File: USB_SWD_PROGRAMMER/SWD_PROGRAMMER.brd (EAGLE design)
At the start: 99.5 x 49.1 mm, 19 parts, among them J1 USB_B, SW1 CJS, SW2 CJS, U1 KW2_CPU_OFFSET, U2 KL20PAD, X1 CSTCE8M00G55-R0

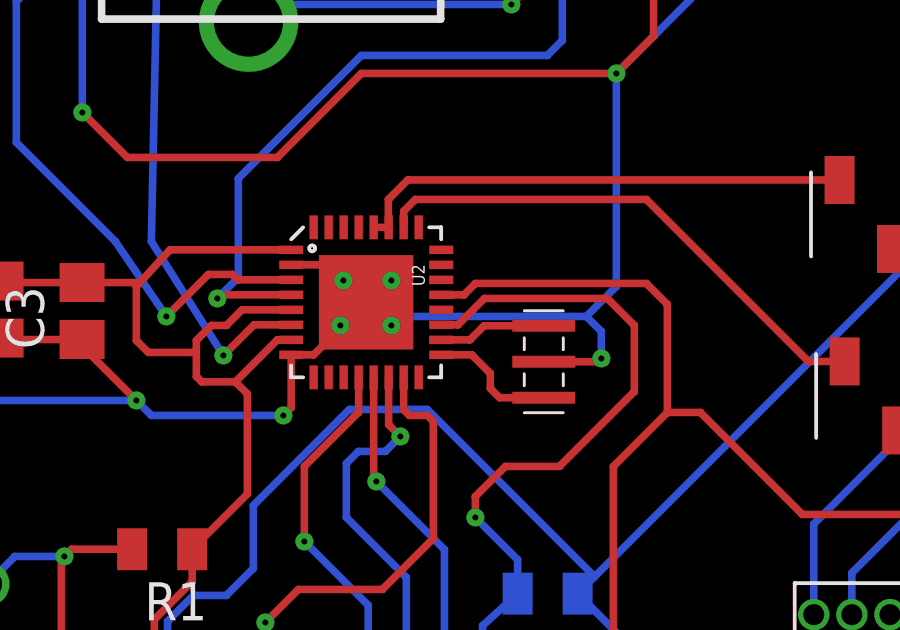
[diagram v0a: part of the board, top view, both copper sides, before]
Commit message: Misc changes (SWD)
Misc changes (SWD)
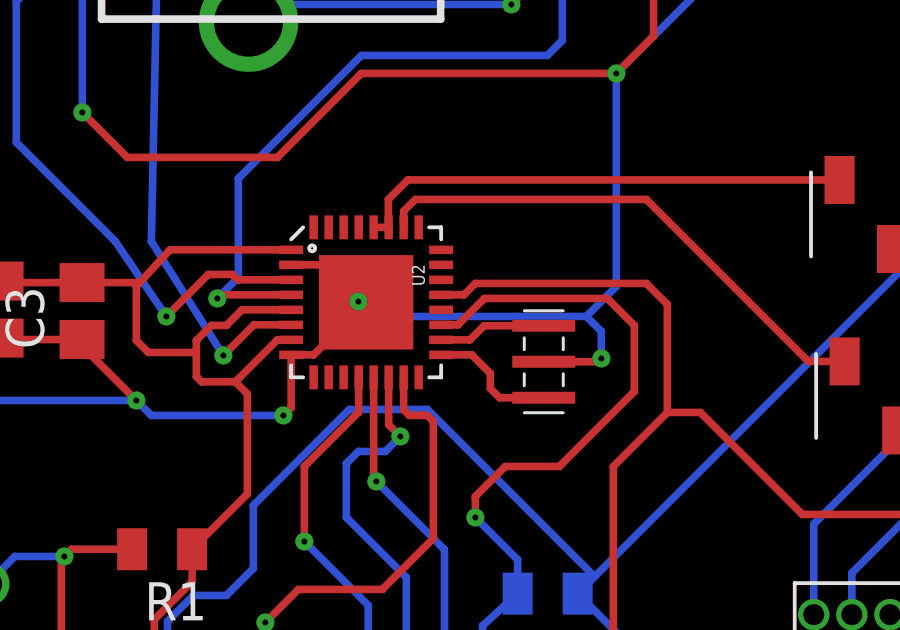
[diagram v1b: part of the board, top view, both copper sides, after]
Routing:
- net GND: track 244.0 -> 244.1 mm, vias 10 -> 7
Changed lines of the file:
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@@
 <?xml version="1.0" encoding="utf-8"?>
 <!DOCTYPE eagle SYSTEM "eagle.dtd">
-<eagle version="7.5.0">
+<eagle version="6.5.0">
 <drawing>
 <settings>
@@
 <pass name="Default">
 <param name="RoutingGrid" value="50mil"/>
-<param name="AutoGrid" value="1"/>
-<param name="Efforts" value="0"/>
-<param name="TopRouterVariant" value="1"/>
 <param name="tpViaShape" value="round"/>
-<param name="PrefDir.1" value="a"/>
+<param name="PrefDir.1" value="|"/>
 <param name="PrefDir.2" value="0"/>
 <param name="PrefDir.3" value="0"/>
@@
 <param name="PrefDir.14" value="0"/>
 <param name="PrefDir.15" value="0"/>
-<param name="PrefDir.16" value="a"/>
+<param name="PrefDir.16" value="-"/>
 <param name="cfVia" value="8"/>
 <param name="cfNonPref" value="5"/>
@@
 <contactref element="U2" pad="EP"/>
 <wire x1="34.26" y1="46.72" x2="35.01" y2="46.72" width="0.254" layer="1"/>
-<wire x1="35.01" y1="46.72" x2="36.76" y2="48.47" width="0.254" layer="1"/>
+<wire x1="35.01" y1="46.72" x2="35.99" y2="47.7" width="0.254" layer="1"/>
+<wire x1="35.99" y1="47.7" x2="36.76" y2="48.47" width="0.254" layer="1"/>
 <wire x1="34.26" y1="49.72" x2="35.51" y2="49.72" width="0.254" layer="1"/>
 <wire x1="35.51" y1="49.72" x2="36.03" y2="49.2" width="0.254" layer="1"/>
-<wire x1="36.03" y1="49.2" x2="36.76" y2="48.47" width="0.254" layer="1"/>
 <wire x1="46.26" y1="65.81" x2="46.26" y2="62.89" width="0.254" layer="1"/>
 <wire x1="46.26" y1="62.89" x2="46.26" y2="59.98" width="0.254" layer="1"/>
 <wire x1="46.26" y1="59.98" x2="46.34" y2="59.9" width="0.254" layer="1"/>
-<via x="37.6" y="47.7" extent="1-16" drill="0.2"/>
-<via x="35.9" y="47.7" extent="1-16" drill="0.2"/>
-<via x="36" y="49.2" extent="1-16" drill="0.2"/>
-<via x="37.6" y="49.2" extent="1-16" drill="0.2"/>
 <wire x1="36" y1="49.2" x2="36.03" y2="49.2" width="0.254" layer="1"/>
-<wire x1="37.6" y1="49.2" x2="37.49" y2="49.2" width="0.254" layer="1"/>
-<wire x1="37.49" y1="49.2" x2="36.76" y2="48.47" width="0.254" layer="1"/>
 <wire x1="37.6" y1="47.7" x2="37.53" y2="47.7" width="0.254" layer="1"/>
-<wire x1="37.53" y1="47.7" x2="36.76" y2="48.47" width="0.254" layer="1"/>
 <wire x1="35.9" y1="47.7" x2="35.99" y2="47.7" width="0.254" layer="1"/>
-<wire x1="35.99" y1="47.7" x2="36.76" y2="48.47" width="0.254" layer="1"/>
 <via x="44.6" y="46.6" extent="1-16" drill="0.2"/>
-<wire x1="44.1" y1="48" x2="37.9" y2="48" width="0.254" layer="16"/>
-<wire x1="37.9" y1="48" x2="37.6" y2="47.7" width="0.254" layer="16"/>
 <wire x1="36.83" y1="34.89" x2="38.1" y2="34.89" width="0.254" layer="16"/>
 <wire x1="38.1" y1="34.89" x2="38.1" y2="31.9" width="0.254" layer="16"/>
@@
 <wire x1="29.1" y1="45.2" x2="27.29" y2="47.01" width="0.254" layer="1"/>
 <wire x1="27.29" y1="47.01" x2="27.29" y2="47.23" width="0.254" layer="1"/>
+<wire x1="44.1" y1="48" x2="37.23" y2="48" width="0.254" layer="16"/>
+<wire x1="37.23" y1="48" x2="36.76" y2="48.47" width="0.254" layer="16"/>
+<via x="36.5" y="48.5" extent="1-16" drill="0.2"/>
+<wire x1="36.5" y1="48.5" x2="36.73" y2="48.5" width="0.254" layer="16"/>
+<wire x1="36.73" y1="48.5" x2="36.76" y2="48.47" width="0.254" layer="16"/>
+<wire x1="36.03" y1="49.2" x2="36.03" y2="48.97" width="0.254" layer="1"/>
+<wire x1="36.03" y1="48.97" x2="36.5" y2="48.5" width="0.254" layer="1"/>
+<wire x1="35.99" y1="47.7" x2="35.99" y2="47.99" width="0.254" layer="1"/>
+<wire x1="35.99" y1="47.99" x2="36.5" y2="48.5" width="0.254" layer="1"/>
+<wire x1="37.53" y1="47.7" x2="37.3" y2="47.7" width="0.254" layer="1"/>
+<wire x1="37.3" y1="47.7" x2="36.5" y2="48.5" width="0.254" layer="1"/>
 </signal>
 <signal name="N$35">

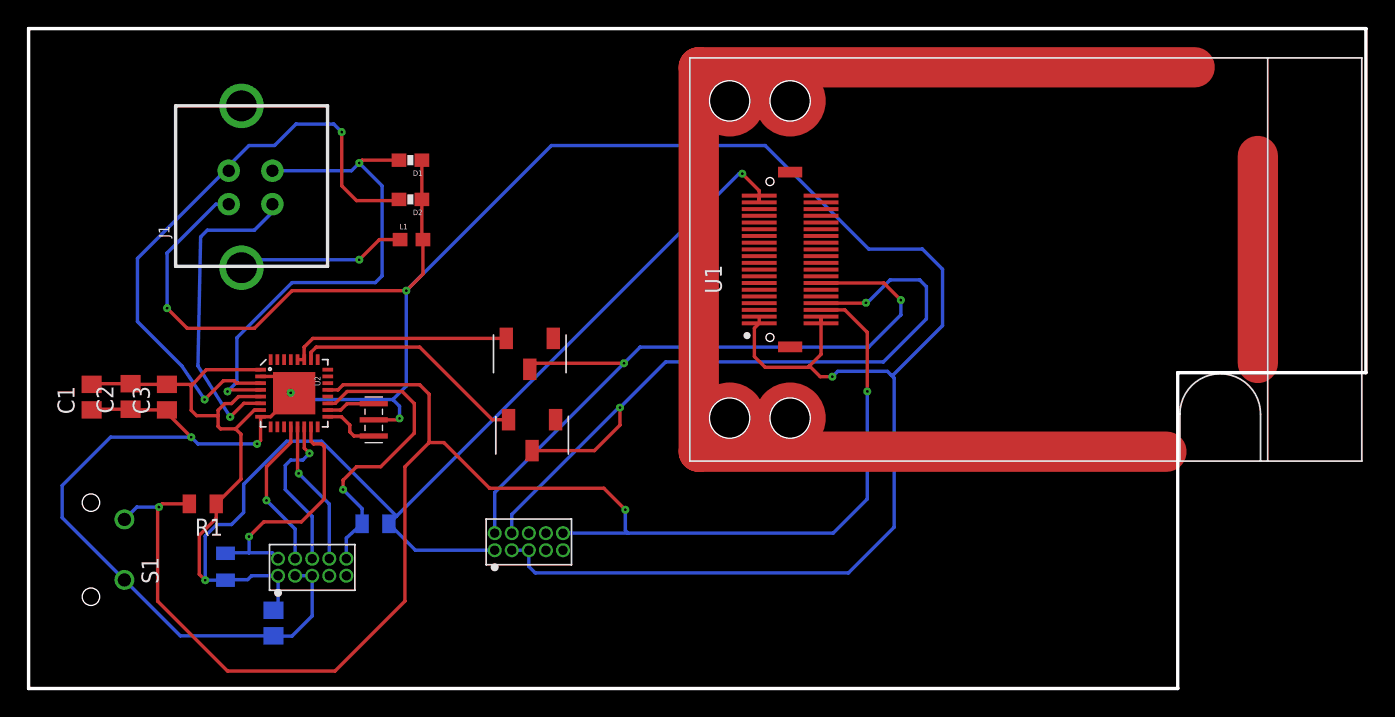
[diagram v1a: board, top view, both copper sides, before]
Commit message: Applied new design rules
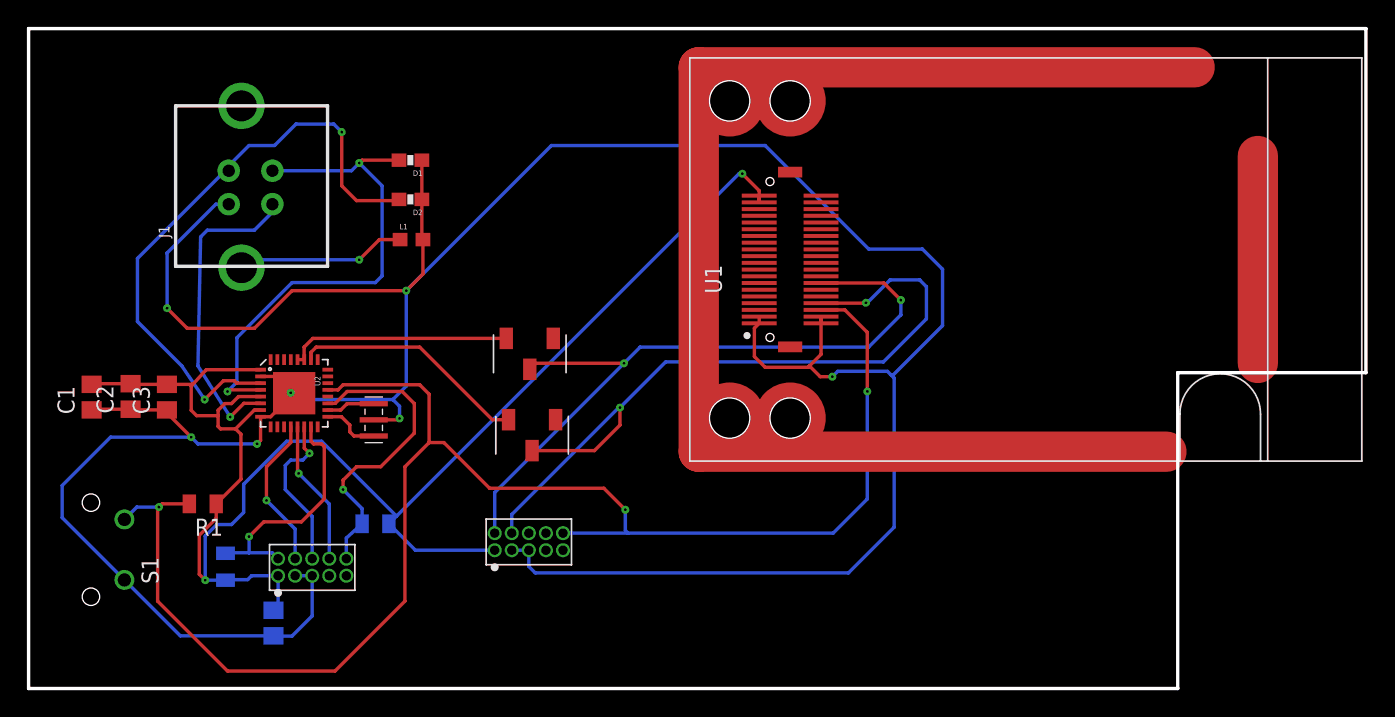
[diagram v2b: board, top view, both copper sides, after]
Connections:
- net N$52 renamed TMS
- net N$55 renamed CLK
- net N$56 renamed TDO
- net N$57 renamed TDI
- net N$58 renamed JRST
- new net N$3: U2.11
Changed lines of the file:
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@@
 </class>
 </classes>
-<designrules name="default *">
-<description language="de">&lt;b&gt;EAGLE Design Rules&lt;/b&gt;
-&lt;p&gt;
-Die Standard-Design-Rules sind so gewählt, dass sie für
-die meisten Anwendungen passen. Sollte ihre Platine
-besondere Anforderungen haben, treffen Sie die erforderlichen
-Einstellungen hier und speichern die Design Rules unter
-einem neuen Namen ab.</description>
+<designrules name="Codeshelf_Standard">
 <description language="en">&lt;b&gt;EAGLE Design Rules&lt;/b&gt;
 &lt;p&gt;
@@
 design rules under a new name.</description>
 <param name="layerSetup" value="(1*16)"/>
-<param name="mtCopper" value="0.035mm 0.035mm 0.035mm 0.035mm 0.035mm 0.035mm 0.035mm 0.035mm 0.035mm 0.035mm 0.035mm 0.035mm 0.035mm 0.035mm 0.035mm 0.035mm"/>
-<param name="mtIsolate" value="1.5mm 0.15mm 0.2mm 0.15mm 0.2mm 0.15mm 0.2mm 0.15mm 0.2mm 0.15mm 0.2mm 0.15mm 0.2mm 0.15mm 0.2mm"/>
-<param name="mdWireWire" value="8mil"/>
-<param name="mdWirePad" value="8mil"/>
-<param name="mdWireVia" value="8mil"/>
-<param name="mdPadPad" value="8mil"/>
-<param name="mdPadVia" value="8mil"/>
-<param name="mdViaVia" value="8mil"/>
-<param name="mdSmdPad" value="8mil"/>
-<param name="mdSmdVia" value="8mil"/>
-<param name="mdSmdSmd" value="8mil"/>
+<param name="mtCopper" value="0.035559375mm 0.035559375mm 0.035559375mm 0.035559375mm 0.0356mm 0.0356mm 0.0356mm 0.0356mm 0.0356mm 0.0356mm 0.0356mm 0.0356mm 0.0356mm 0.0356mm 0.035559375mm 0.035559375mm"/>
+<param name="mtIsolate" value="1.47mm 38mil 10mil 0.1499mm 0.2007mm 0.1499mm 0.2007mm 0.1499mm 0.2007mm 0.1499mm 0.2007mm 0.1499mm 0.2007mm 0.1499mm 10mil"/>
+<param name="mdWireWire" value="0.2mm"/>
+<param name="mdWirePad" value="0.2mm"/>
+<param name="mdWireVia" value="0.2mm"/>
+<param name="mdPadPad" value="0.2mm"/>
+<param name="mdPadVia" value="0.2mm"/>
+<param name="mdViaVia" value="0.2mm"/>
+<param name="mdSmdPad" value="0mil"/>
+<param name="mdSmdVia" value="0mil"/>
+<param name="mdSmdSmd" value="0mil"/>
 <param name="mdViaViaSameLayer" value="8mil"/>
 <param name="mnLayersViaInSmd" value="2"/>
-<param name="mdCopperDimension" value="40mil"/>
-<param name="mdDrill" value="8mil"/>
+<param name="mdCopperDimension" value="0.4mm"/>
+<param name="mdDrill" value="0.5mm"/>
 <param name="mdSmdStop" value="0mil"/>
-<param name="msWidth" value="10mil"/>
-<param name="msDrill" value="24mil"/>
-<param name="msMicroVia" value="9.99mm"/>
+<param name="msWidth" value="0.2mm"/>
+<param name="msDrill" value="0.25mm"/>
+<param name="msMicroVia" value="9.9898mm"/>
 <param name="msBlindViaRatio" value="0.5"/>
 <param name="rvPadTop" value="0.25"/>
@@
 <param name="rvMicroViaOuter" value="0.25"/>
 <param name="rvMicroViaInner" value="0.25"/>
-<param name="rlMinPadTop" value="1mil"/>
-<param name="rlMaxPadTop" value="20mil"/>
-<param name="rlMinPadInner" value="1mil"/>
-<param name="rlMaxPadInner" value="20mil"/>
-<param name="rlMinPadBottom" value="1mil"/>
-<param name="rlMaxPadBottom" value="20mil"/>
-<param name="rlMinViaOuter" value="8mil"/>
-<param name="rlMaxViaOuter" value="20mil"/>
-<param name="rlMinViaInner" value="8mil"/>
-<param name="rlMaxViaInner" value="20mil"/>
-<param name="rlMinMicroViaOuter" value="4mil"/>
-<param name="rlMaxMicroViaOuter" value="20mil"/>
-<param name="rlMinMicroViaInner" value="4mil"/>
-<param name="rlMaxMicroViaInner" value="20mil"/>
+<param name="rlMinPadTop" value="0.15mm"/>
+<param name="rlMaxPadTop" value="2mm"/>
+<param name="rlMinPadInner" value="0.15mm"/>
+<param name="rlMaxPadInner" value="2mm"/>
+<param name="rlMinPadBottom" value="0.15mm"/>
+<param name="rlMaxPadBottom" value="2mm"/>
+<param name="rlMinViaOuter" value="0.2mm"/>
+<param name="rlMaxViaOuter" value="2mm"/>
+<param name="rlMinViaInner" value="0.2mm"/>
+<param name="rlMaxViaInner" value="2mm"/>
+<param name="rlMinMicroViaOuter" value="0.1mm"/>
+<param name="rlMaxMicroViaOuter" value="1mm"/>
+<param name="rlMinMicroViaInner" value="0.1mm"/>
+<param name="rlMaxMicroViaInner" value="1mm"/>
 <param name="psTop" value="-1"/>
 <param name="psBottom" value="-1"/>
@@
 <param name="mvStopFrame" value="1"/>
 <param name="mvCreamFrame" value="0"/>
-<param name="mlMinStopFrame" value="4mil"/>
-<param name="mlMaxStopFrame" value="4mil"/>
+<param name="mlMinStopFrame" value="0.05mm"/>
+<param name="mlMaxStopFrame" value="0.05mm"/>
 <param name="mlMinCreamFrame" value="0mil"/>
 <param name="mlMaxCreamFrame" value="0mil"/>
-<param name="mlViaStopLimit" value="0mil"/>
+<param name="mlViaStopLimit" value="0.5mm"/>
 <param name="srRoundness" value="0"/>
 <param name="srMinRoundness" value="0mil"/>
 <param name="srMaxRoundness" value="0mil"/>
-<param name="slThermalIsolate" value="10mil"/>
-<param name="slThermalsForVias" value="0"/>
-<param name="dpMaxLengthDifference" value="10mm"/>
+<param name="slThermalIsolate" value="0.25mm"/>
+<param name="slThermalsForVias" value="1"/>
+<param name="dpMaxLengthDifference" value="1mm"/>
 <param name="dpGapFactor" value="2.5"/>
-<param name="checkGrid" value="0"/>
-<param name="checkAngle" value="0"/>
+<param name="checkGrid" value="1"/>
+<param name="checkAngle" value="1"/>
 <param name="checkFont" value="1"/>
 <param name="checkRestrict" value="1"/>
@@
 <wire x1="33.43" y1="58.4" x2="32.84" y2="69.85" width="0" layer="19" extent="16-16"/>
 </signal>
-<signal name="N$52">
+<signal name="TMS">
 <contactref element="JP2" pad="P$2"/>
 <contactref element="R3" pad="2"/>
@@
 <wire x1="38.8" y1="44.7" x2="39" y2="44.5" width="0.254" layer="1"/>
 </signal>
-<signal name="N$55">
+<signal name="CLK">
 <contactref element="JP2" pad="P$4"/>
 <contactref element="U2" pad="12"/>
@@
 <wire x1="36.51" y1="44.81" x2="36.51" y2="45.97" width="0.254" layer="1"/>
 </signal>
-<signal name="N$56">
+<signal name="TDO">
 <contactref element="JP2" pad="P$6"/>
 <contactref element="U2" pad="14"/>
@@
 <wire x1="37.51" y1="44.39" x2="37.9" y2="44" width="0.254" layer="1"/>
 </signal>
-<signal name="N$57">
+<signal name="TDI">
 <contactref element="U2" pad="13"/>
 <contactref element="JP2" pad="P$8"/>
@@
 <wire x1="37.01" y1="42.59" x2="37.01" y2="45.97" width="0.254" layer="1"/>
 </signal>
-<signal name="N$58">
+<signal name="JRST">
 <contactref element="U2" pad="19"/>
 <contactref element="R2" pad="2"/>
@@
 <wire x1="33.02" y1="47.72" x2="32" y2="46.7" width="0.254" layer="1"/>
 </signal>
+<signal name="N$3">
+<contactref element="U2" pad="11"/>
+</signal>
 </signals>

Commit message: Messing w/ Programmer
Tweaking USB
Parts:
- added JP3: (no value), pinhead:1X11
- moved S1 2.35 mm to (21.9, 36.2), turned to 270 degrees
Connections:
- new net N$7: JP3.5, U2.5
- new net N$8: JP3.6, U2.6
- net +3V3: now also JP3.10, JP3.11, JP3.9; no longer U2.5
- net GND: now also JP3.1, JP3.2, JP3.3
- net JRST: now also JP3.8
- net N$2: now also JP3.7; no longer U2.6
- net N$3: now also JP3.4
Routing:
- net N$8: track 0.00 -> 98.1 mm, vias 0 -> 3
- net N$7: track 0.00 -> 98.1 mm, vias 0 -> 3
- net N$2: track 23.5 -> 111.7 mm, vias 1 -> 0
- net N$3: track 0.00 -> 69.5 mm, vias 0 -> 1
- net JRST: track 23.1 -> 59.9 mm
- net GND: track 244.1 -> 268.6 mm, vias 7 -> 6
- net +3V3: track 119.9 -> 135.2 mm
- net RST: track 117.9 -> 125.1 mm
- net N$36: track 45.8 -> 44.9 mm
